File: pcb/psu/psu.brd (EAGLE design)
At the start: 86.4 x 54.7 mm, 31 parts, among them U1 EEPROM-I2CSMD, U2 LM2596, U3 LM2596

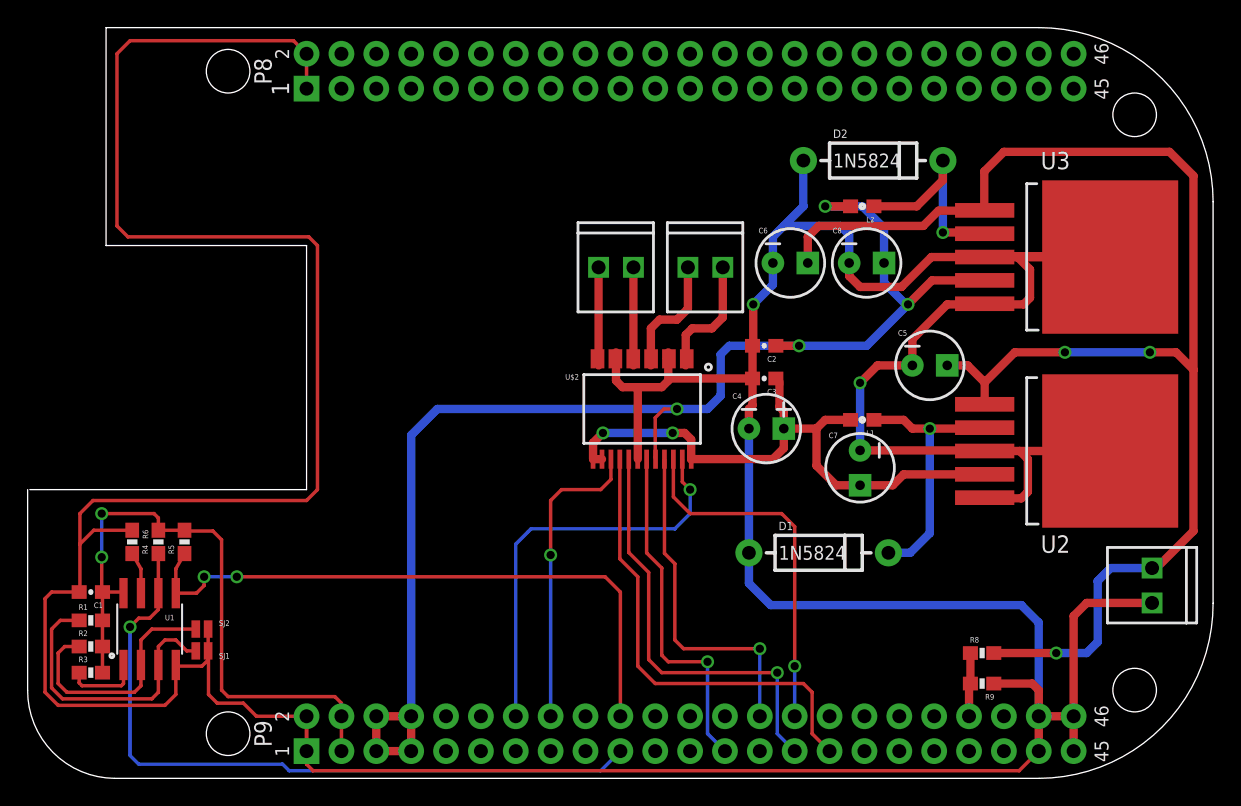
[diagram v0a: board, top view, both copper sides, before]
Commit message: Updated board layout with ground pours
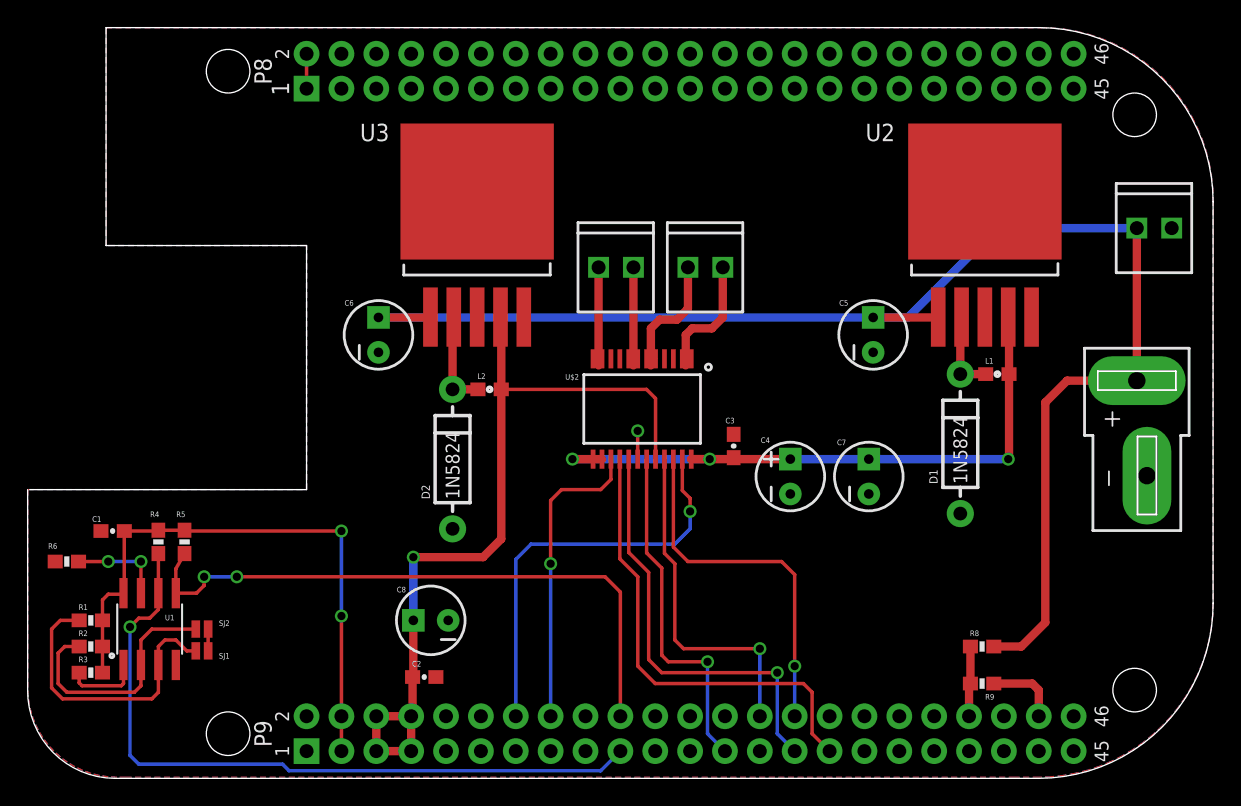
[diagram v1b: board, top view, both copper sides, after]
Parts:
- added J1: BATTERY_CONNDEANS, SparkFun-Connectors:DEANS
- moved U3 56.8 mm to (27.1, 47.6), turned to 0 degrees
- moved C8 41.1 mm to (29.4, 11.4), turned to 180 degrees
- moved D2 37.6 mm to (31.0, 23.2), turned to 90 degrees
- moved C2 34.6 mm to (28.9, 7.30), turned to 0 degrees
- moved C6 30.5 mm to (25.6, 32.2), turned to 90 degrees
- moved L2 30.2 mm to (33.7, 28.3), turned to 0 degrees
- moved U2 26.8 mm to (64.1, 47.6), turned to 0 degrees
- moved JP1 24.8 mm to (80.8, 40.0), turned to 0 degrees
- moved D1 13.0 mm to (67.9, 24.3), turned to 90 degrees
- moved L1 10.4 mm to (70.6, 29.4), turned to 0 degrees
- moved C3 5.40 mm to (51.4, 24.1), turned to 90 degrees
- moved R6 4.97 mm to (2.86, 15.7), turned to 0 degrees
- moved C1 4.72 mm to (6.19, 17.9)
- moved C5 4.69 mm to (61.6, 32.2), turned to 90 degrees
- moved C4 3.90 mm to (55.6, 21.9), turned to 90 degrees
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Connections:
- net GND: now also J1.-
- net V_BATT: now also J1.+
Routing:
- net GND: track 399.6 -> 12.0 mm, vias 2 -> 1
- net V_CPU: track 98.6 -> 60.9 mm, vias 4 -> 1
- net N$8: track 19.6 -> 6.04 mm, vias 1 -> 0
- net N$9: track 15.6 -> 7.12 mm, vias 1 -> 0
- net N$5: track 3.05 -> 6.85 mm, vias 0 -> 2
- net 3.3V: track 47.0 -> 43.5 mm
- net V_BATT: track 103.2 -> 105.4 mm, vias 3 -> 0
- net V_MOTOR: track 44.5 -> 45.9 mm, vias 2 -> 3
- added copper zone on layer 1, net GND
- added copper zone on layer 16, net GND
